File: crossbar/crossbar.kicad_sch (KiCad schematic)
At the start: 23 parts, among them J1 Conn_02x06_Counter_Clockwise, J10 Conn_02x12_Row_Letter_First, J11 Conn_02x06_Counter_Clockwise, J12 Conn_02x06_Counter_Clockwise, J13 Conn_02x06_Counter_Clockwise, J14 Conn_02x06_Counter_Clockwise, J15 Conn_02x06_Counter_Clockwise, J2 Conn_02x06_Counter_Clockwise, J3 Conn_02x06_Counter_Clockwise, J4 Conn_02x06_Counter_Clockwise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

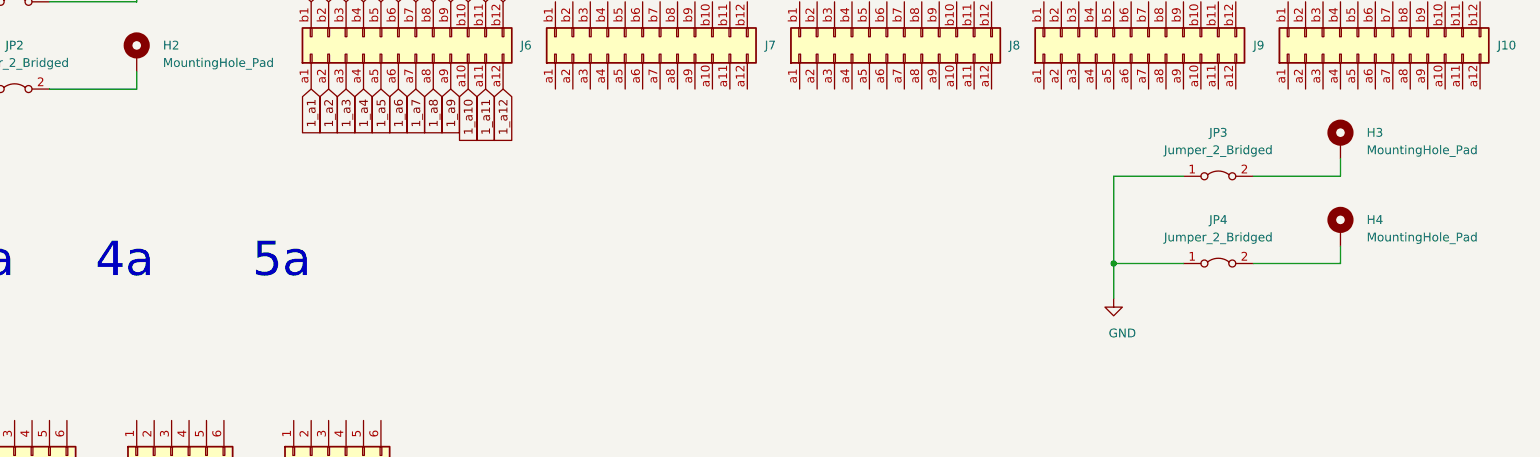
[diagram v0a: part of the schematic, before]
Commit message: redesign adapter mount
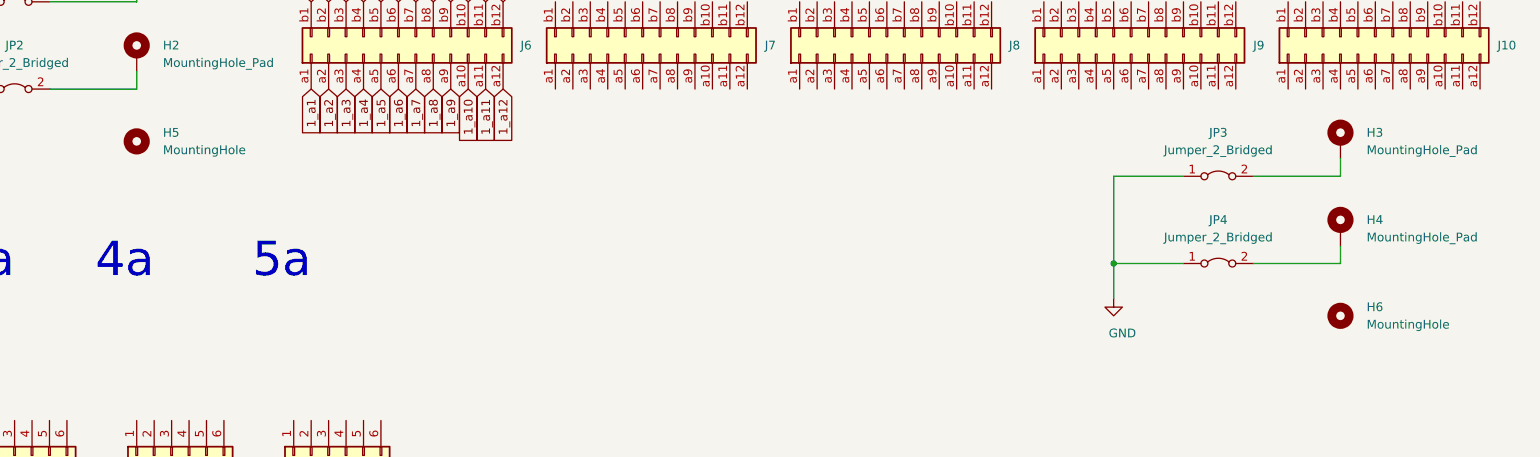
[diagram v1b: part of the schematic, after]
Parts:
- added H5, H6: MountingHole, MountingHole:MountingHole_3mm, symbol Mechanical:MountingHole
- J10, J6, J7, J8, J9: footprint MINE:PinSocket_2x12_P2.00mm_Vertical_EDGE_USBC_pins -> MINE:TMM-112-01-STRADDLE; ptno (none) -> TMM-112-01-T-D
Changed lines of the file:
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@@
     (pin "1")
+  )
+  (symbol (lib_id "Mechanical:MountingHole") (at 83.82 111.76 0) (unit 1)
+    (in_bom yes) (on_board yes)
+    (property "Reference" "H5" (id 0) (at 87.63 110.49 0)
+      (effects (font (size 1.27 1.27)) (justify left))
+    )
+    (property "Value" "MountingHole" (id 1) (at 87.63 113.03 0)
+      (effects (font (size 1.27 1.27)) (justify left))
+    )
+    (property "Footprint" "MountingHole:MountingHole_3mm" (id 2) (at 83.82 111.76 0)
+      (effects (font (size 1.27 1.27)) hide)
+    )
+    (property "Datasheet" "~" (id 3) (at 83.82 111.76 0)
+      (effects (font (size 1.27 1.27)) hide)
+    )
+  )
+  (symbol (lib_id "Mechanical:MountingHole") (at 259.08 137.16 0) (unit 1)
+    (in_bom yes) (on_board yes)
+    (property "Reference" "H6" (id 0) (at 262.89 135.89 0)
+      (effects (font (size 1.27 1.27)) (justify left))
+    )
+    (property "Value" "MountingHole" (id 1) (at 262.89 138.43 0)
+      (effects (font (size 1.27 1.27)) (justify left))
+    )
+    (property "Footprint" "MountingHole:MountingHole_3mm" (id 2) (at 259.08 137.16 0)
+      (effects (font (size 1.27 1.27)) hide)
+    )
+    (property "Datasheet" "~" (id 3) (at 259.08 137.16 0)
+      (effects (font (size 1.27 1.27)) hide)
+    )
   )
   (symbol (lib_id "Mechanical:MountingHole_Pad") (at 83.82 86.36 0) (unit 1)
@@
       (effects (font (size 1.27 1.27)) (justify right) hide)
     )
-    (property "Footprint" "MINE:PinSocket_2x12_P2.00mm_Vertical_EDGE_USBC_pins" (id 2) (at 121.92 99.06 0)
+    (property "Footprint" "MINE:TMM-112-01-STRADDLE" (id 2) (at 121.92 99.06 0)
       (effects (font (size 1.27 1.27)) hide)
     )
     (property "Datasheet" "~" (id 3) (at 121.92 99.06 0)
+      (effects (font (size 1.27 1.27)) hide)
+    )
+    (property "ptno" "TMM-112-01-T-D" (id 4) (at 121.92 99.06 90)
       (effects (font (size 1.27 1.27)) hide)
     )
@@
       (effects (font (size 1.27 1.27)) (justify right) hide)
     )
-    (property "Footprint" "MINE:PinSocket_2x12_P2.00mm_Vertical_EDGE_USBC_pins" (id 2) (at 157.48 99.06 0)
+    (property "Footprint" "MINE:TMM-112-01-STRADDLE" (id 2) (at 157.48 99.06 0)
       (effects (font (size 1.27 1.27)) hide)
     )
     (property "Datasheet" "~" (id 3) (at 157.48 99.06 0)
+      (effects (font (size 1.27 1.27)) hide)
+    )
+    (property "ptno" "TMM-112-01-T-D" (id 4) (at 157.48 99.06 90)
       (effects (font (size 1.27 1.27)) hide)
     )
@@
       (effects (font (size 1.27 1.27)) (justify right) hide)
     )
-    (property "Footprint" "MINE:PinSocket_2x12_P2.00mm_Vertical_EDGE_USBC_pins" (id 2) (at 193.04 99.06 0)
+    (property "Footprint" "MINE:TMM-112-01-STRADDLE" (id 2) (at 193.04 99.06 0)
       (effects (font (size 1.27 1.27)) hide)
     )
     (property "Datasheet" "~" (id 3) (at 193.04 99.06 0)
+      (effects (font (size 1.27 1.27)) hide)
+    )
+    (property "ptno" "TMM-112-01-T-D" (id 4) (at 193.04 99.06 90)
       (effects (font (size 1.27 1.27)) hide)
     )
@@
       (effects (font (size 1.27 1.27)) (justify right) hide)
     )
-    (property "Footprint" "MINE:PinSocket_2x12_P2.00mm_Vertical_EDGE_USBC_pins" (id 2) (at 228.6 99.06 0)
+    (property "Footprint" "MINE:TMM-112-01-STRADDLE" (id 2) (at 228.6 99.06 0)
       (effects (font (size 1.27 1.27)) hide)
     )
     (property "Datasheet" "~" (id 3) (at 228.6 99.06 0)
+      (effects (font (size 1.27 1.27)) hide)
+    )
+    (property "ptno" "TMM-112-01-T-D" (id 4) (at 228.6 99.06 90)
       (effects (font (size 1.27 1.27)) hide)
     )
@@
       (effects (font (size 1.27 1.27)) (justify right) hide)
     )
-    (property "Footprint" "MINE:PinSocket_2x12_P2.00mm_Vertical_EDGE_USBC_pins" (id 2) (at 264.16 99.06 0)
+    (property "Footprint" "MINE:TMM-112-01-STRADDLE" (id 2) (at 264.16 99.06 0)
       (effects (font (size 1.27 1.27)) hide)
     )
     (property "Datasheet" "~" (id 3) (at 264.16 99.06 0)
+      (effects (font (size 1.27 1.27)) hide)
+    )
+    (property "ptno" "TMM-112-01-T-D" (id 4) (at 264.16 99.06 90)
       (effects (font (size 1.27 1.27)) hide)
     )
@@
       (reference "H4") (unit 1) (value "MountingHole_Pad") (footprint "MountingHole:MountingHole_2.2mm_M2_Pad_Via")
     )
+    (path "/bb82cea9-66a3-42fb-b058-3e7c37ed1670"
+      (reference "H5") (unit 1) (value "MountingHole") (footprint "MountingHole:MountingHole_3mm")
+    )
+    (path "/3902802f-b718-4a19-a5bf-f0f1780c200b"
+      (reference "H6") (unit 1) (value "MountingHole") (footprint "MountingHole:MountingHole_3mm")
+    )
     (path "/eaee8da0-fb99-43be-b9ee-57fb8a40fab1"
       (reference "J1") (unit 1) (value "Conn_02x06_Counter_Clockwise") (footprint "MINE:71609")
@@
     )
     (path "/c5e268d7-b843-4262-9142-450e3d58f6e6"
-      (reference "J6") (unit 1) (value "Conn_02x12_Row_Letter_First") (footprint "MINE:PinSocket_2x12_P2.00mm_Vertical_EDGE_USBC_pins")
+      (reference "J6") (unit 1) (value "Conn_02x12_Row_Letter_First") (footprint "MINE:TMM-112-01-STRADDLE")
     )
     (path "/384045dc-b2d9-4f45-a413-7ba83d46608a"
-      (reference "J7") (unit 1) (value "Conn_02x12_Row_Letter_First") (footprint "MINE:PinSocket_2x12_P2.00mm_Vertical_EDGE_USBC_pins")
+      (reference "J7") (unit 1) (value "Conn_02x12_Row_Letter_First") (footprint "MINE:TMM-112-01-STRADDLE")
     )
     (path "/2bc25a0b-6b50-4c81-92c9-d57190c795bd"
-      (reference "J8") (unit 1) (value "Conn_02x12_Row_Letter_First") (footprint "MINE:PinSocket_2x12_P2.00mm_Vertical_EDGE_USBC_pins")
+      (reference "J8") (unit 1) (value "Conn_02x12_Row_Letter_First") (footprint "MINE:TMM-112-01-STRADDLE")
     )
     (path "/81d9d38b-bc4e-4d24-9d44-f87043ca7ae7"
-      (reference "J9") (unit 1) (value "Conn_02x12_Row_Letter_First") (footprint "MINE:PinSocket_2x12_P2.00mm_Vertical_EDGE_USBC_pins")
+      (reference "J9") (unit 1) (value "Conn_02x12_Row_Letter_First") (footprint "MINE:TMM-112-01-STRADDLE")
     )
     (path "/96e42f0c-d8db-4326-8efd-a763f64f4871"
-      (reference "J10") (unit 1) (value "Conn_02x12_Row_Letter_First") (footprint "MINE:PinSocket_2x12_P2.00mm_Vertical_EDGE_USBC_pins")
+      (reference "J10") (unit 1) (value "Conn_02x12_Row_Letter_First") (footprint "MINE:TMM-112-01-STRADDLE")
     )
     (path "/6d194ca0-2dd7-480b-a787-a851080092a5"

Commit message: wip on 4x1 crossbar
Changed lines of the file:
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@@
     (effects (font (size 5 5)) (justify right bottom))
   )
-  (text "2b" (at 45.72 22.86 180)
-    (effects (font (size 5 5)) (justify right bottom))
-  )
-  (text "2a" (at 45.72 132.08 180)
-    (effects (font (size 5 5)) (justify right bottom))
-  )
-  (text "3b" (at 66.04 22.86 180)
-    (effects (font (size 5 5)) (justify right bottom))
-  )
-  (text "3a" (at 66.04 132.08 180)
-    (effects (font (size 5 5)) (justify right bottom))
-  )
-  (text "4b" (at 86.36 22.86 180)
-    (effects (font (size 5 5)) (justify right bottom))
-  )
-  (text "4a" (at 86.36 132.08 180)
-    (effects (font (size 5 5)) (justify right bottom))
-  )
-  (text "5b" (at 109.22 22.86 180)
-    (effects (font (size 5 5)) (justify right bottom))
-  )
-  (text "5a" (at 109.22 132.08 180)
+  (text "2a" (at 48.26 132.08 180)
+    (effects (font (size 5 5)) (justify right bottom))
+  )
+  (text "2b" (at 50.8 22.86 180)
+    (effects (font (size 5 5)) (justify right bottom))
+  )
+  (text "3a" (at 71.12 132.08 180)
+    (effects (font (size 5 5)) (justify right bottom))
+  )
+  (text "3b" (at 73.66 22.86 180)
+    (effects (font (size 5 5)) (justify right bottom))
+  )
+  (text "4a" (at 93.98 132.08 180)
+    (effects (font (size 5 5)) (justify right bottom))
+  )
+  (text "4b" (at 96.52 22.86 180)
+    (effects (font (size 5 5)) (justify right bottom))
+  )
+  (text "5a" (at 116.84 132.08 180)
+    (effects (font (size 5 5)) (justify right bottom))
+  )
+  (text "5b" (at 119.38 22.86 180)
     (effects (font (size 5 5)) (justify right bottom))
   )
@@
     )
     (property "Datasheet" "" (id 3) (at 226.06 134.62 0)
-      (effects (font (size 1.27 1.27)) hide)
-    )
-    (pin "1")
-  )
-  (symbol (lib_id "Mechanical:MountingHole") (at 83.82 111.76 0) (unit 1)
-    (in_bom yes) (on_board yes)
-    (property "Reference" "H5" (id 0) (at 87.63 110.49 0)
-      (effects (font (size 1.27 1.27)) (justify left))
-    )
-    (property "Value" "MountingHole" (id 1) (at 87.63 113.03 0)
-      (effects (font (size 1.27 1.27)) (justify left))
-    )
-    (property "Footprint" "MountingHole:MountingHole_3mm" (id 2) (at 83.82 111.76 0)
-      (effects (font (size 1.27 1.27)) hide)
-    )
-    (property "Datasheet" "~" (id 3) (at 83.82 111.76 0)
-      (effects (font (size 1.27 1.27)) hide)
-    )
-  )
-  (symbol (lib_id "Mechanical:MountingHole") (at 259.08 137.16 0) (unit 1)
-    (in_bom yes) (on_board yes)
-    (property "Reference" "H6" (id 0) (at 262.89 135.89 0)
-      (effects (font (size 1.27 1.27)) (justify left))
-    )
-    (property "Value" "MountingHole" (id 1) (at 262.89 138.43 0)
-      (effects (font (size 1.27 1.27)) (justify left))
-    )
-    (property "Footprint" "MountingHole:MountingHole_3mm" (id 2) (at 259.08 137.16 0)
-      (effects (font (size 1.27 1.27)) hide)
-    )
-    (property "Datasheet" "~" (id 3) (at 259.08 137.16 0)
-      (effects (font (size 1.27 1.27)) hide)
-    )
-  )
-  (symbol (lib_id "Mechanical:MountingHole_Pad") (at 83.82 86.36 0) (unit 1)
-    (in_bom yes) (on_board yes)
-    (property "Reference" "H1" (id 0) (at 87.63 85.09 0)
-      (effects (font (size 1.27 1.27)) (justify left))
-    )
-    (property "Value" "MountingHole_Pad" (id 1) (at 87.63 87.63 0)
-      (effects (font (size 1.27 1.27)) (justify left))
-    )
-    (property "Footprint" "MountingHole:MountingHole_2.2mm_M2_Pad_Via" (id 2) (at 83.82 86.36 0)
-      (effects (font (size 1.27 1.27)) hide)
-    )
-    (property "Datasheet" "~" (id 3) (at 83.82 86.36 0)
-      (effects (font (size 1.27 1.27)) hide)
-    )
-    (pin "1")
-  )
-  (symbol (lib_id "Mechanical:MountingHole_Pad") (at 83.82 99.06 0) (unit 1)
-    (in_bom yes) (on_board yes)
-    (property "Reference" "H2" (id 0) (at 87.63 97.79 0)
-      (effects (font (size 1.27 1.27)) (justify left))
-    )
-    (property "Value" "MountingHole_Pad" (id 1) (at 87.63 100.33 0)
-      (effects (font (size 1.27 1.27)) (justify left))
-    )
-    (property "Footprint" "MountingHole:MountingHole_2.2mm_M2_Pad_Via" (id 2) (at 83.82 99.06 0)
-      (effects (font (size 1.27 1.27)) hide)
-    )
-    (property "Datasheet" "~" (id 3) (at 83.82 99.06 0)
-      (effects (font (size 1.27 1.27)) hide)
-    )
-    (pin "1")
-  )
-  (symbol (lib_id "Mechanical:MountingHole_Pad") (at 259.08 111.76 0) (unit 1)
-    (in_bom yes) (on_board yes)
-    (property "Reference" "H3" (id 0) (at 262.89 110.49 0)
-      (effects (font (size 1.27 1.27)) (justify left))
-    )
-    (property "Value" "MountingHole_Pad" (id 1) (at 262.89 113.03 0)
-      (effects (font (size 1.27 1.27)) (justify left))
-    )
-    (property "Footprint" "MountingHole:MountingHole_2.2mm_M2_Pad_Via" (id 2) (at 259.08 111.76 0)
-      (effects (font (size 1.27 1.27)) hide)
-    )
-    (property "Datasheet" "~" (id 3) (at 259.08 111.76 0)
-      (effects (font (size 1.27 1.27)) hide)
-    )
-    (pin "1")
-  )
-  (symbol (lib_id "Mechanical:MountingHole_Pad") (at 259.08 124.46 0) (unit 1)
-    (in_bom yes) (on_board yes)
-    (property "Reference" "H4" (id 0) (at 262.89 123.19 0)
-      (effects (font (size 1.27 1.27)) (justify left))
-    )
-    (property "Value" "MountingHole_Pad" (id 1) (at 262.89 125.73 0)
-      (effects (font (size 1.27 1.27)) (justify left))
-    )
-    (property "Footprint" "MountingHole:MountingHole_2.2mm_M2_Pad_Via" (id 2) (at 259.08 124.46 0)
-      (effects (font (size 1.27 1.27)) hide)
-    )
-    (property "Datasheet" "~" (id 3) (at 259.08 124.46 0)
       (effects (font (size 1.27 1.27)) hide)
     )
@@
     (pin "2")
   )
+  (symbol (lib_id "Mechanical:MountingHole") (at 83.82 111.76 0) (unit 1)
+    (in_bom yes) (on_board yes)
+    (property "Reference" "H5" (id 0) (at 87.63 110.49 0)
+      (effects (font (size 1.27 1.27)) (justify left))
+    )
+    (property "Value" "MountingHole" (id 1) (at 87.63 113.03 0)
+      (effects (font (size 1.27 1.27)) (justify left))
+    )
+    (property "Footprint" "MountingHole:MountingHole_3mm" (id 2) (at 83.82 111.76 0)
+      (effects (font (size 1.27 1.27)) hide)
+    )
+    (property "Datasheet" "~" (id 3) (at 83.82 111.76 0)
+      (effects (font (size 1.27 1.27)) hide)
+    )
+  )
+  (symbol (lib_id "Mechanical:MountingHole") (at 259.08 137.16 0) (unit 1)
+    (in_bom yes) (on_board yes)
+    (property "Reference" "H6" (id 0) (at 262.89 135.89 0)
+      (effects (font (size 1.27 1.27)) (justify left))
+    )
+    (property "Value" "MountingHole" (id 1) (at 262.89 138.43 0)
+      (effects (font (size 1.27 1.27)) (justify left))
+    )
+    (property "Footprint" "MountingHole:MountingHole_3mm" (id 2) (at 259.08 137.16 0)
+      (effects (font (size 1.27 1.27)) hide)
+    )
+    (property "Datasheet" "~" (id 3) (at 259.08 137.16 0)
+      (effects (font (size 1.27 1.27)) hide)
+    )
+  )
+  (symbol (lib_id "Mechanical:MountingHole_Pad") (at 83.82 86.36 0) (unit 1)
+    (in_bom yes) (on_board yes)
+    (property "Reference" "H1" (id 0) (at 87.63 85.09 0)
+      (effects (font (size 1.27 1.27)) (justify left))
+    )
+    (property "Value" "MountingHole_Pad" (id 1) (at 87.63 87.63 0)
+      (effects (font (size 1.27 1.27)) (justify left))
+    )
+    (property "Footprint" "MountingHole:MountingHole_2.2mm_M2_Pad_Via" (id 2) (at 83.82 86.36 0)
+      (effects (font (size 1.27 1.27)) hide)
+    )
+    (property "Datasheet" "~" (id 3) (at 83.82 86.36 0)
+      (effects (font (size 1.27 1.27)) hide)
+    )
+    (pin "1")
+  )
+  (symbol (lib_id "Mechanical:MountingHole_Pad") (at 83.82 99.06 0) (unit 1)
+    (in_bom yes) (on_board yes)
+    (property "Reference" "H2" (id 0) (at 87.63 97.79 0)
+      (effects (font (size 1.27 1.27)) (justify left))
+    )
+    (property "Value" "MountingHole_Pad" (id 1) (at 87.63 100.33 0)
+      (effects (font (size 1.27 1.27)) (justify left))
+    )
+    (property "Footprint" "MountingHole:MountingHole_2.2mm_M2_Pad_Via" (id 2) (at 83.82 99.06 0)
+      (effects (font (size 1.27 1.27)) hide)
+    )
+    (property "Datasheet" "~" (id 3) (at 83.82 99.06 0)
+      (effects (font (size 1.27 1.27)) hide)
+    )
+    (pin "1")
+  )
+  (symbol (lib_id "Mechanical:MountingHole_Pad") (at 259.08 111.76 0) (unit 1)
+    (in_bom yes) (on_board yes)
+    (property "Reference" "H3" (id 0) (at 262.89 110.49 0)
+      (effects (font (size 1.27 1.27)) (justify left))
+    )
+    (property "Value" "MountingHole_Pad" (id 1) (at 262.89 113.03 0)
+      (effects (font (size 1.27 1.27)) (justify left))
+    )
+    (property "Footprint" "MountingHole:MountingHole_2.2mm_M2_Pad_Via" (id 2) (at 259.08 111.76 0)
+      (effects (font (size 1.27 1.27)) hide)
+    )
+    (property "Datasheet" "~" (id 3) (at 259.08 111.76 0)
+      (effects (font (size 1.27 1.27)) hide)
+    )
+    (pin "1")
+  )
+  (symbol (lib_id "Mechanical:MountingHole_Pad") (at 259.08 124.46 0) (unit 1)
+    (in_bom yes) (on_board yes)
+    (property "Reference" "H4" (id 0) (at 262.89 123.19 0)
+      (effects (font (size 1.27 1.27)) (justify left))
+    )
+    (property "Value" "MountingHole_Pad" (id 1) (at 262.89 125.73 0)
+      (effects (font (size 1.27 1.27)) (justify left))
+    )
+    (property "Footprint" "MountingHole:MountingHole_2.2mm_M2_Pad_Via" (id 2) (at 259.08 124.46 0)
+      (effects (font (size 1.27 1.27)) hide)
+    )
+    (property "Datasheet" "~" (id 3) (at 259.08 124.46 0)
+      (effects (font (size 1.27 1.27)) hide)
+    )
+    (pin "1")
+  )
   (symbol (lib_id "Connector_Generic:Conn_02x06_Counter_Clockwise") (at 20.32 43.18 90) (mirror x) (unit 1)
